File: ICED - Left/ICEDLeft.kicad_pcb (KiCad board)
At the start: 2 copper layers, 160.2 x 145 mm, 164 parts, among them P1 FLASH_HDR, P2 USBC, P3 CONN_17, P4 USB3_AFEMALE, Q1 TC1264, U1 MK20DX256VLH7, U2 IS31FL3731C, X1 CRYSTAL

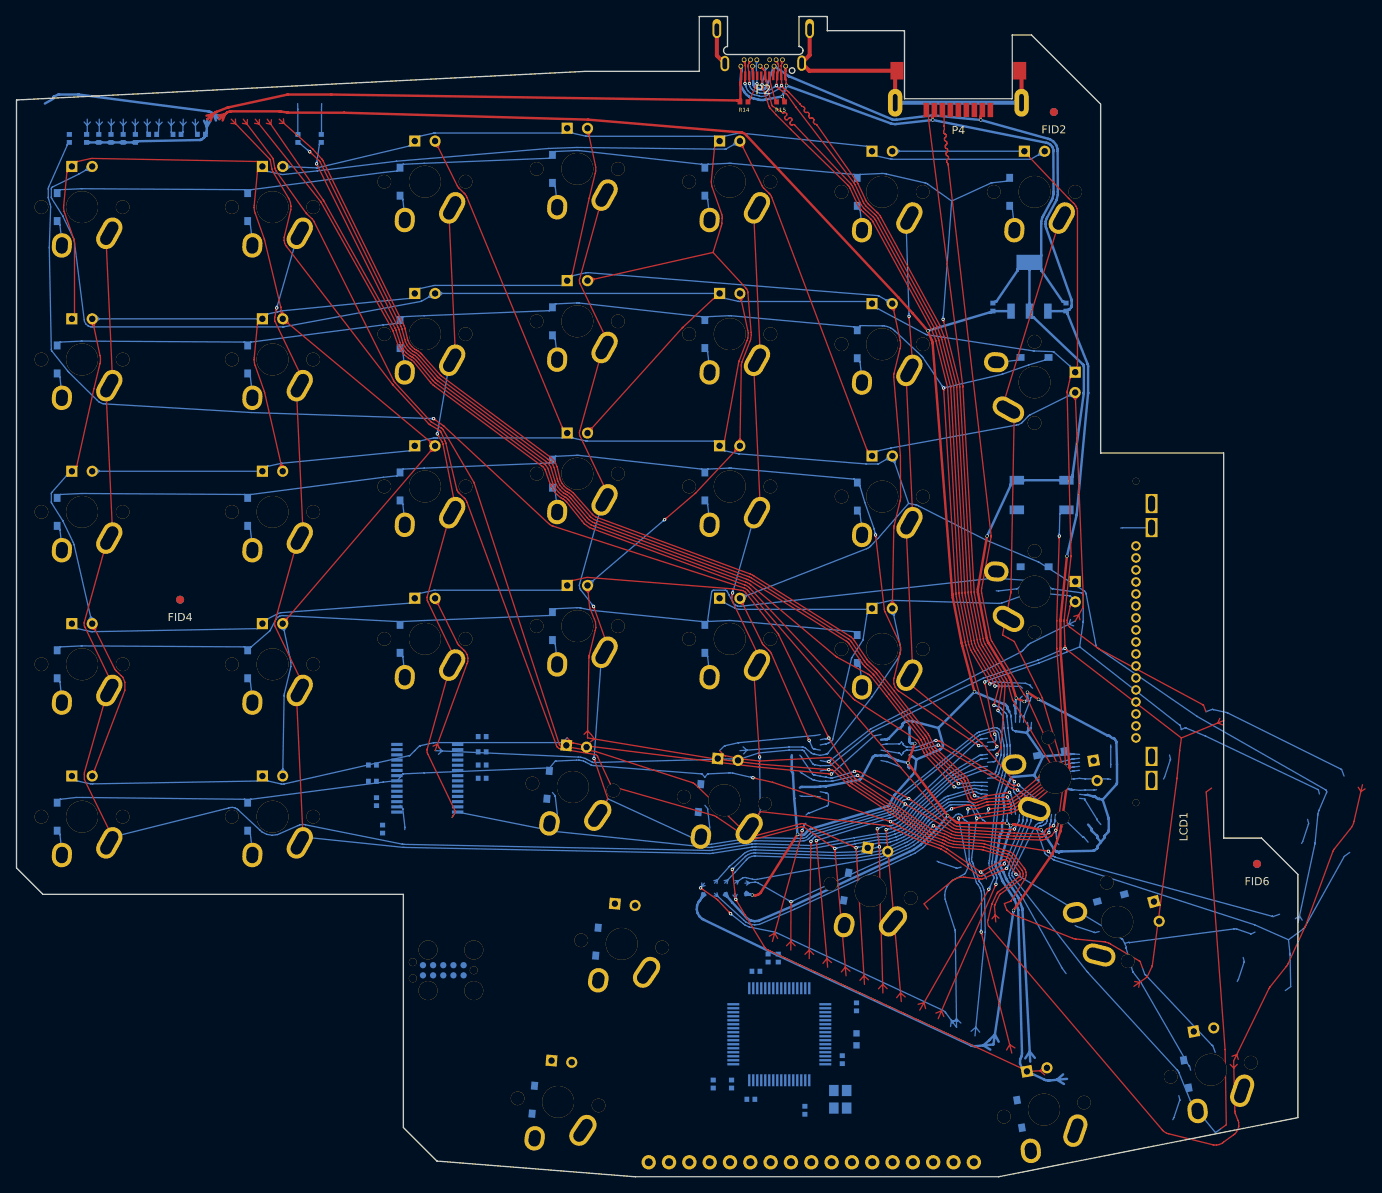
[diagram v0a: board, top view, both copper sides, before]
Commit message: moved LCD components R13, C17, and C16
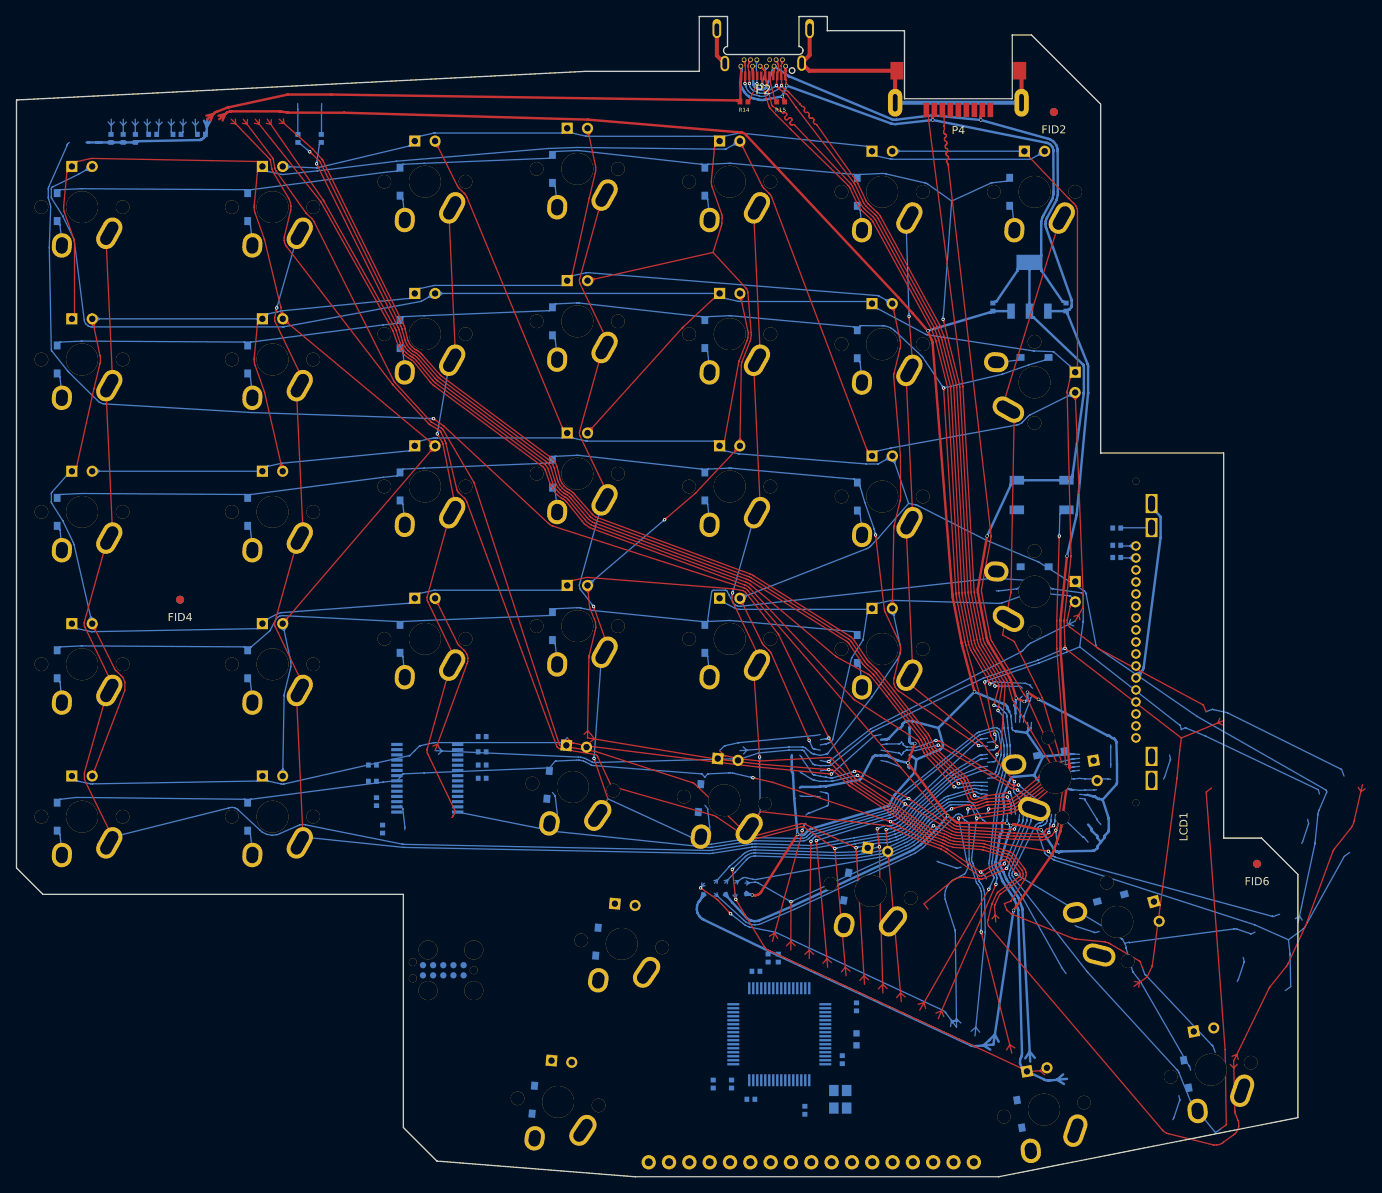
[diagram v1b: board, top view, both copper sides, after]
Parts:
- moved R13 139.7 mm to (155.2, 89.7), turned to 450 degrees
- moved C17 138.4 mm to (155.2, 91.9), turned to 270 degrees
- moved C16 137.6 mm to (155.2, 93.4), turned to 270 degrees
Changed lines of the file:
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@@
   )
   (module prettylib:SMD-1005 (layer Back)
-    (at 26.416 41.021)
+    (at 155.18 91.88 270)
     (attr smd)
-    (fp_text reference C17 (at 0 1.778 90) (layer B.SilkS)
+    (fp_text reference C17 (at 0 1.778 0) (layer B.SilkS)
       (effects (font (size 0.508 0.508) (thickness 0.127)) (justify mirror))
     )
-    (fp_text value 1uF (at 0.889 0 270) (layer B.SilkS) hide
+    (fp_text value 1uF (at 0.889 0 540) (layer B.SilkS) hide
       (effects (font (size 0.508 0.508) (thickness 0.127)) (justify mirror))
     )
@@
     (fp_line (start -0.5 -0.95) (end -0.5 0.95) (layer Cmts.User) (width 0.05))
     (fp_line (start -0.5 0.95) (end 0.5 0.95) (layer Cmts.User) (width 0.05))
-    (pad 1 smd rect (at 0 0.5) (size 0.65 0.6) (layers Back B.Paste B.Mask)
+    (pad 1 smd rect (at 0 0.5 270) (size 0.65 0.6) (layers Back B.Paste B.Mask)
       (net 34 VSS))
-    (pad 2 smd rect (at 0 -0.5) (size 0.65 0.6) (layers Back B.Paste B.Mask)
+    (pad 2 smd rect (at 0 -0.5 270) (size 0.65 0.6) (layers Back B.Paste B.Mask)
       (net 48 "Net-(C17-Pad2)"))
   )
   (module prettylib:SMD-1005 (layer Back)
-    (at 27.94 41.021)
+    (at 155.18 93.404 270)
     (attr smd)
-    (fp_text reference C16 (at 0 1.778 90) (layer B.SilkS)
+    (fp_text reference C16 (at 0 1.778 0) (layer B.SilkS)
       (effects (font (size 0.508 0.508) (thickness 0.127)) (justify mirror))
     )
-    (fp_text value 1uF (at 0.889 0 270) (layer B.SilkS) hide
+    (fp_text value 1uF (at 0.889 0 540) (layer B.SilkS) hide
       (effects (font (size 0.508 0.508) (thickness 0.127)) (justify mirror))
     )
@@
     (fp_line (start -0.5 -0.95) (end -0.5 0.95) (layer Cmts.User) (width 0.05))
     (fp_line (start -0.5 0.95) (end 0.5 0.95) (layer Cmts.User) (width 0.05))
-    (pad 1 smd rect (at 0 0.5) (size 0.65 0.6) (layers Back B.Paste B.Mask)
+    (pad 1 smd rect (at 0 0.5 270) (size 0.65 0.6) (layers Back B.Paste B.Mask)
       (net 34 VSS))
-    (pad 2 smd rect (at 0 -0.5) (size 0.65 0.6) (layers Back B.Paste B.Mask)
+    (pad 2 smd rect (at 0 -0.5 270) (size 0.65 0.6) (layers Back B.Paste B.Mask)
       (net 47 "Net-(C16-Pad2)"))
   )
@@
   )
   (module prettylib:SMD-1005 (layer Back)
-    (at 24.257 41.021 180)
+    (at 155.18 89.721 450)
     (attr smd)
-    (fp_text reference R13 (at 0 1.524 180) (layer B.SilkS)
+    (fp_text reference R13 (at 0 1.524 450) (layer B.SilkS)
       (effects (font (size 0.508 0.508) (thickness 0.127)) (justify mirror))
     )
-    (fp_text value 33 (at 0.889 0 450) (layer B.SilkS) hide
+    (fp_text value 33 (at 0.889 0 720) (layer B.SilkS) hide
       (effects (font (size 0.508 0.508) (thickness 0.127)) (justify mirror))
     )
@@
     (fp_line (start -0.5 -0.95) (end -0.5 0.95) (layer Cmts.User) (width 0.05))
     (fp_line (start -0.5 0.95) (end 0.5 0.95) (layer Cmts.User) (width 0.05))
-    (pad 1 smd rect (at 0 0.5 180) (size 0.65 0.6) (layers Back B.Paste B.Mask)
+    (pad 1 smd rect (at 0 0.5 450) (size 0.65 0.6) (layers Back B.Paste B.Mask)
       (net 89 "Net-(LCD1-Pad2)"))
-    (pad 2 smd rect (at 0 -0.5 180) (size 0.65 0.6) (layers Back B.Paste B.Mask)
+    (pad 2 smd rect (at 0 -0.5 450) (size 0.65 0.6) (layers Back B.Paste B.Mask)
       (net 15 /mcu/LCD_KR))
   )
@@
   (segment (start 129.4256 118.2826) (end 129.578 118.2826) (width 0.3048) (layer Back) (net 33))
   (segment (start 129.278 118.11) (end 129.4256 118.2826) (width 0.3048) (layer Back) (net 33))
-  (segment (start 22.2446 36.0674) (end 21.197 36.665) (width 0.3048) (layer Back) (net 33))
-  (segment (start 22.2446 35.915) (end 22.2446 36.0674) (width 0.3048) (layer Back) (net 33))
-  (segment (start 22.2446 35.8687) (end 22.2446 35.915) (width 0.3048) (layer Back) (net 33))
-  (segment (start 22.2961 35.7918) (end 22.2446 35.8687) (width 0.3048) (layer Back) (net 33))
-  (segment (start 22.3389 35.7741) (end 22.2961 35.7918) (width 0.3048) (layer Back) (net 33))
-  (segment (start 22.8517 35.5627) (end 22.3389 35.7741) (width 0.3048) (layer Back) (net 33))
-  (segment (start 22.8863 35.5484) (end 22.8517 35.5627) (width 0.3048) (layer Back) (net 33))
-  (segment (start 22.9596 35.5339) (end 22.8863 35.5484) (width 0.3048) (layer Back) (net 33))
-  (segment (start 22.997 35.5339) (end 22.9596 35.5339) (width 0.3048) (layer Back) (net 33))
-  (segment (start 25.397 35.5339) (end 22.997 35.5339) (width 0.3048) (layer Back) (net 33))
-  (segment (start 25.4091 35.5339) (end 25.397 35.5339) (width 0.3048) (layer Back) (net 33))
-  (segment (start 25.4337 35.5355) (end 25.4091 35.5339) (width 0.3048) (layer Back) (net 33))
-  (segment (start 25.4462 35.5371) (end 25.4337 35.5355) (width 0.3048) (layer Back) (net 33))
-  (segment (start 41.6236 37.6421) (end 25.4462 35.5371) (width 0.3048) (layer Back) (net 33))
-  (segment (start 41.7662 37.6606) (end 41.6236 37.6421) (width 0.3048) (layer Back) (net 33))
-  (segment (start 42.0291 37.7782) (end 41.7662 37.6606) (width 0.3048) (layer Back) (net 33))
-  (segment (start 42.1387 37.8729) (end 42.0291 37.7782) (width 0.3048) (layer Back) (net 33))
-  (segment (start 42.997 38.615) (end 42.1387 37.8729) (width 0.3048) (layer Back) (net 33))
+  (segment (start 160.133 87.708) (end 159.536 86.661) (width 0.3048) (layer Back) (net 33))
+  (segment (start 160.667 88.315) (end 160.133 87.708) (width 0.3048) (layer Back) (net 33))
+  (segment (start 160.667 90.91) (end 160.667 88.315) (width 0.3048) (layer Back) (net 33))
+  (segment (start 158.559 107.087) (end 160.667 90.91) (width 0.3048) (layer Back) (net 33))
+  (segment (start 158.54 107.23) (end 158.559 107.087) (width 0.3048) (layer Back) (net 33))
+  (segment (start 158.423 107.493) (end 158.54 107.23) (width 0.3048) (layer Back) (net 33))
+  (segment (start 157.586 108.461) (end 158.423 107.493) (width 0.3048) (layer Back) (net 33))
+  (segment (start 158.217 107.73) (end 158.022 108.563) (width 0.3048) (layer Back) (net 33))
+  (segment (start 158.217 107.73) (end 157.422 108.044) (width 0.3048) (layer Back) (net 33))
   (segment (start 114.8655 123.517) (end 115.28 128.005) (width 0.3048) (layer Back) (net 33))
   (segment (start 114.8644 123.5014) (end 114.8655 123.517) (width 0.3048) (layer Back) (net 33))
@@
   (segment (start 135.7894 104.0828) (end 135.8681 104.4247) (width 0.3048) (layer Front) (net 33))
   (segment (start 137.402 110.199) (end 135.8681 104.4247) (width 0.3048) (layer Front) (net 33))
-  (segment (start 42.2664 37.9834) (end 43.0995 38.1793) (width 0.3048) (layer Back) (net 33))
-  (segment (start 42.2664 37.9834) (end 42.5807 38.7793) (width 0.3048) (layer Back) (net 33))
   (segment (start 140.9292 126.3307) (end 140.9191 126.4967) (width 0.1524) (layer Back) (net 33))
   (segment (start 140.9292 126.3307) (end 140.7969 126.4313) (width 0.1524) (layer Back) (net 33))
@@
   (segment (start 29.497 39.3979) (end 29.1077 38.9655) (width 0.1524) (layer Back) (net 46))
   (segment (start 29.497 39.3979) (end 29.8863 38.9655) (width 0.1524) (layer Back) (net 46))
-  (segment (start 27.997 40.221) (end 27.997 38.615) (width 0.1524) (layer Back) (net 47))
-  (segment (start 27.997 40.2972) (end 27.997 40.221) (width 0.1524) (layer Back) (net 47))
-  (segment (start 27.94 40.521) (end 27.997 40.2972) (width 0.1524) (layer Back) (net 47))
-  (segment (start 27.997 39.3979) (end 27.6077 38.9655) (width 0.1524) (layer Back) (net 47))
-  (segment (start 27.997 39.3979) (end 28.3863 38.9655) (width 0.1524) (layer Back) (net 47))
-  (segment (start 26.497 40.221) (end 26.497 38.615) (width 0.1524) (layer Back) (net 48))
-  (segment (start 26.497 40.2972) (end 26.497 40.221) (width 0.1524) (layer Back) (net 48))
-  (segment (start 26.416 40.521) (end 26.497 40.2972) (width 0.1524) (layer Back) (net 48))
-  (segment (start 26.497 39.3979) (end 26.1077 38.9655) (width 0.1524) (layer Back) (net 48))
-  (segment (start 26.497 39.3979) (end 26.8863 38.9655) (width 0.1524) (layer Back) (net 48))
+  (segment (start 155.904 93.461) (end 157.586 93.461) (width 0.1524) (layer Back) (net 47))
+  (segment (start 155.68 93.404) (end 155.904 93.461) (width 0.1524) (layer Back) (net 47))
+  (segment (start 156.803 93.461) (end 157.235 93.071) (width 0.1524) (layer Back) (net 47))
+  (segment (start 156.803 93.461) (end 157.235 93.85) (width 0.1524) (layer Back) (net 47))
+  (segment (start 155.904 91.961) (end 157.586 91.961) (width 0.1524) (layer Back) (net 48))
+  (segment (start 155.68 91.88) (end 155.904 91.961) (width 0.1524) (layer Back) (net 48))
+  (segment (start 156.803 91.961) (end 157.235 91.571) (width 0.1524) (layer Back) (net 48))
+  (segment (start 156.803 91.961) (end 157.235 92.35) (width 0.1524) (layer Back) (net 48))
   (segment (start 142.1453 49.8729) (end 141.796 49.4487) (width 0.1524) (layer Back) (net 49))
   (segment (start 142.1453 49.9491) (end 142.1453 49.8729) (width 0.1524) (layer Back) (net 49))

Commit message: moved the rest of the LCD resisters and capaciters
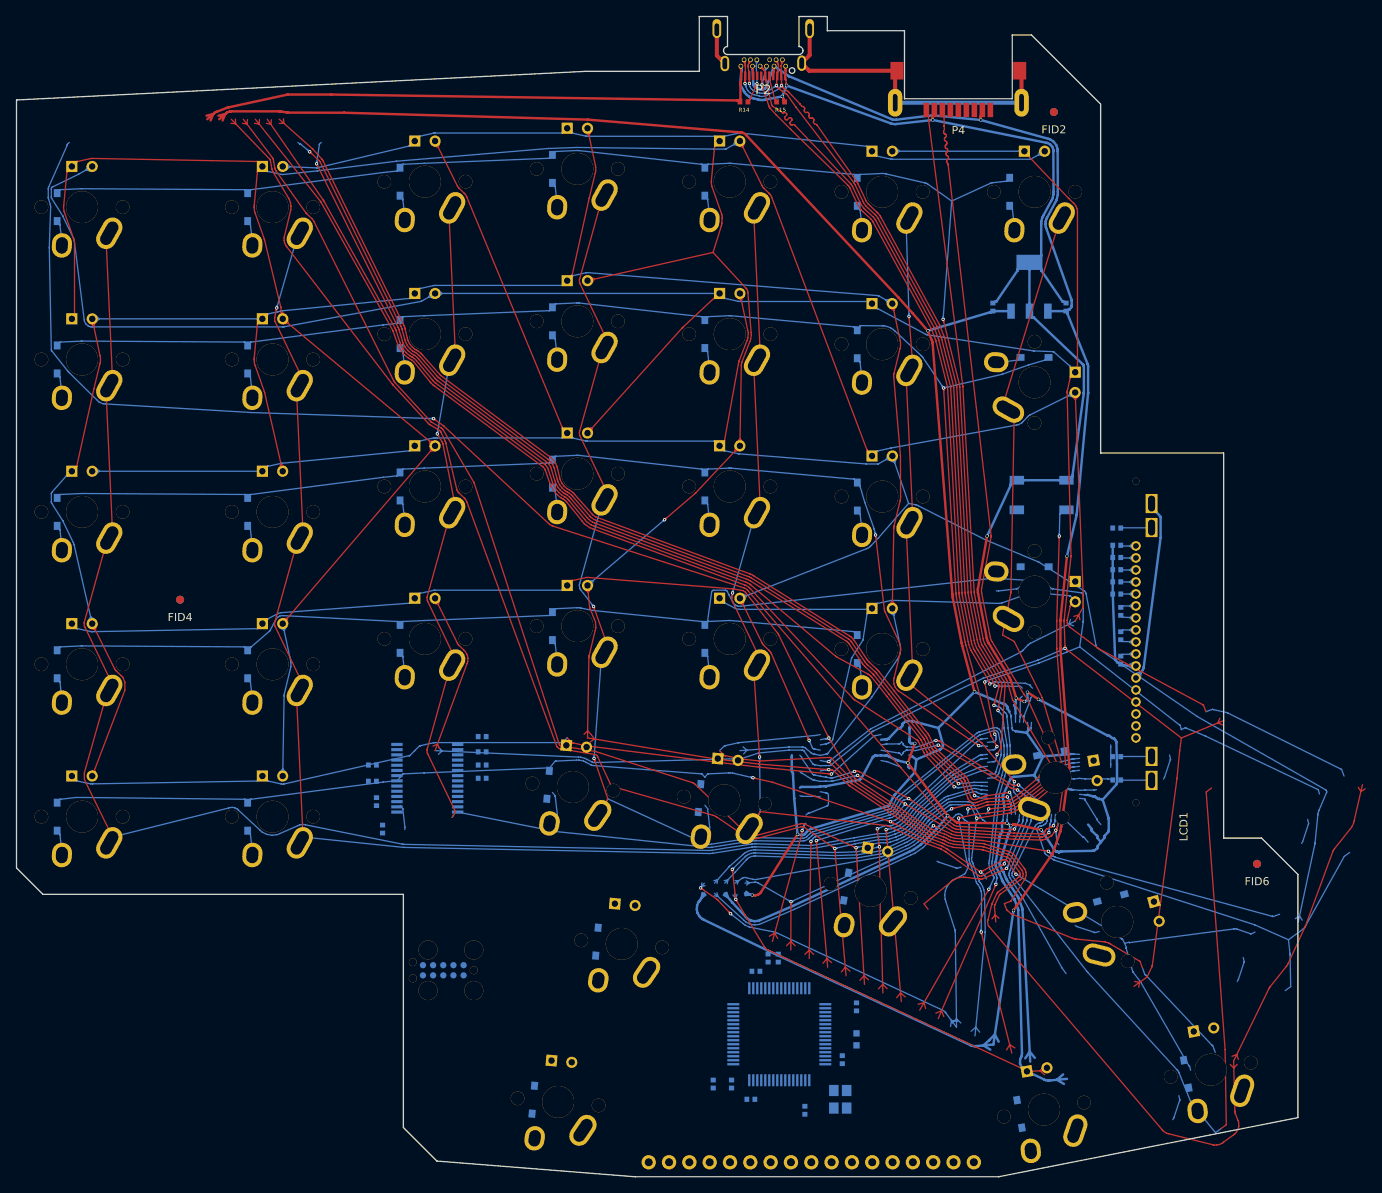
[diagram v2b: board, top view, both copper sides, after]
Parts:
- moved C15 136.8 mm to (155.2, 94.9), turned to 270 degrees
- moved C14 136.0 mm to (155.2, 96.5), turned to 270 degrees
- moved C13 135.2 mm to (155.2, 98.0), turned to 270 degrees
- moved C12 134.9 mm to (155.7, 100.1), turned to 0 degrees
- moved C11 133.6 mm to (155.7, 103.2), turned to 0 degrees
- moved C10 132.4 mm to (155.7, 106.2), turned to 180 degrees
- moved R10 128.2 mm to (155.2, 118.3), turned to 90 degrees
- moved R9 127.7 mm to (155.2, 121.2), turned to 90 degrees
